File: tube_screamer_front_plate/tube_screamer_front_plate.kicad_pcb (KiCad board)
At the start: 2 copper layers, 80 x 100 mm, 12 parts, among them J1 top_panel_connector

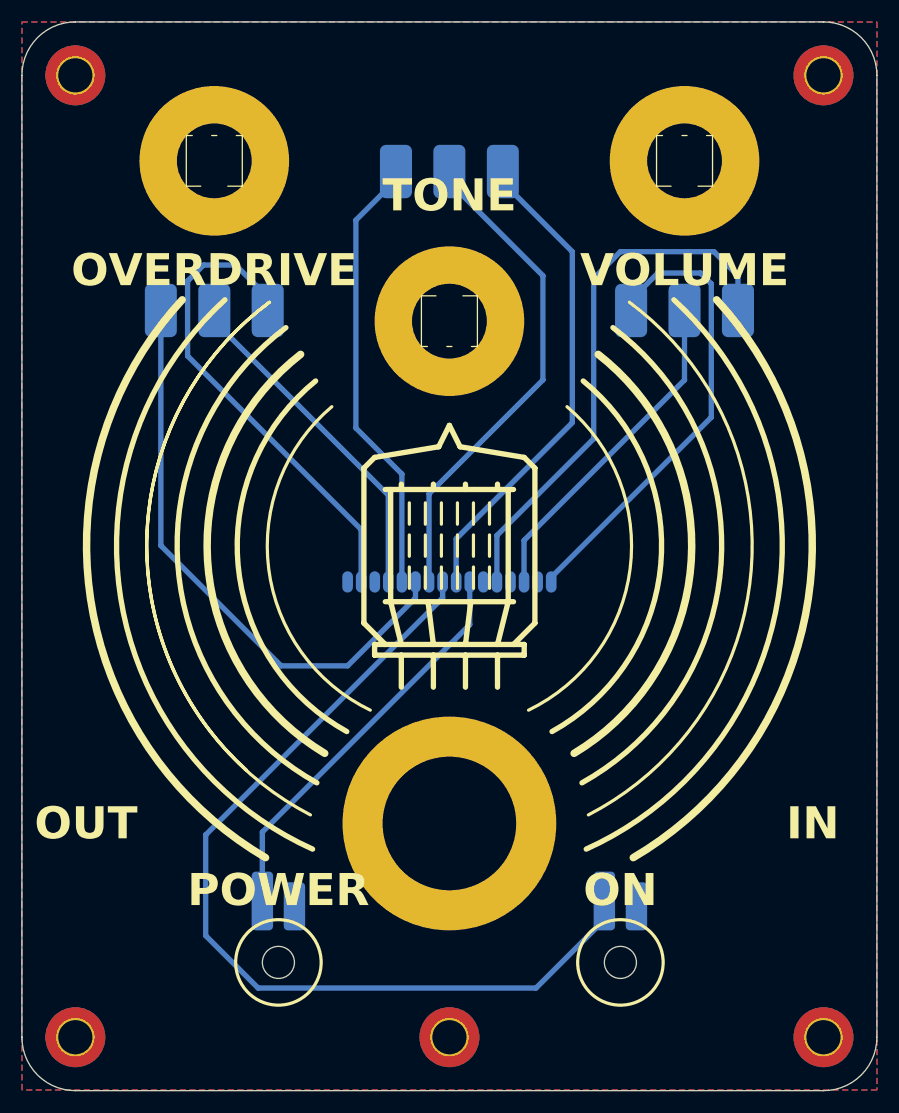
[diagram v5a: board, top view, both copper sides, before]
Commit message: Tube screamer front plate done, library updated.
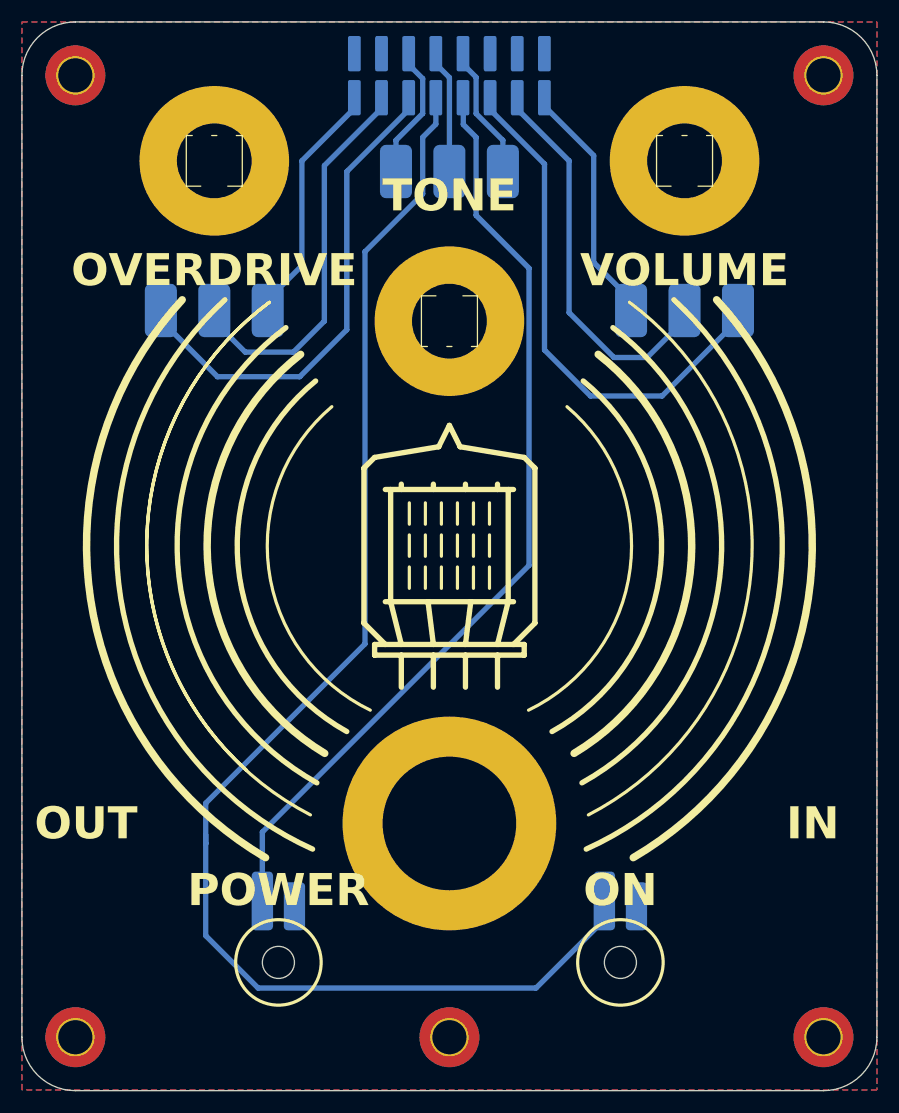
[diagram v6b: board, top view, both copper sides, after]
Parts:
- J1: footprint pedale:bottom_connector -> pedale:IDC-Header_2x08_faux_SMD
- moved J1 48.7 mm to (81.1, 53.7)
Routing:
- net Net-(D2-A): track 37.9 -> 88.1 mm
- net Net-(D1-A): track 86.0 -> 131.9 mm
- net Net-(J1B-Pin_7): track 46.4 -> 11.6 mm
- net Net-(J1B-Pin_9): track 45.6 -> 12.6 mm
- net Net-(J1B-Pin_5): track 41.7 -> 12.6 mm
- net Net-(J1A-Pin_2): track 45.5 -> 23.3 mm
- net Net-(J1C-Pin_16): track 44.1 -> 23.3 mm
- net Net-(J1A-Pin_6): track 54.6 -> 46.4 mm
- net Net-(J1C-Pin_14): track 31.6 -> 37.0 mm
- net Net-(J1A-Pin_4): track 32.5 -> 36.8 mm
- net Net-(J1C-Pin_12): track 50.9 -> 48.0 mm

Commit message: GND to top.
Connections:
- J1 pad 3: unconnected-(J1F-GND-Pad3) -> 0

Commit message: Added label to front plate botom.
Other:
- board text added: "100 kOhm lin"
- board text added: "20 kOhm lin"
- board text added: "500 kOhm log"
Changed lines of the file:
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@@
 			(at 1.27 6.1 90)
 			(layer "B.SilkS")
+			(hide yes)
 			(effects
 				(font
@@
 		)
 	)
+	(gr_text "100 kOhm lin\n"
+		(at 116.8 82.85 0)
+		(layer "B.SilkS")
+		(effects
+			(font
+				(size 1 1)
+				(thickness 0.15)
+			)
+			(justify left bottom mirror)
+		)
+	)
+	(gr_text "20 kOhm lin\n"
+		(at 94.4 89 0)
+		(layer "B.SilkS")
+		(effects
+			(font
+				(size 1 1)
+				(thickness 0.15)
+			)
+			(justify left bottom mirror)
+		)
+	)
+	(gr_text "500 kOhm log\n"
+		(at 73.55 82.9 0)
+		(layer "B.SilkS")
+		(effects
+			(font
+				(size 1 1)
+				(thickness 0.15)
+			)
+			(justify left bottom mirror)
+		)
+	)
